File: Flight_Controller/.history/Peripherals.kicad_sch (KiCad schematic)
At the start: 56 parts, among them IC1 AT7456E, U2 BMI270, U3 TLV75533PDBV, U4 W25Q128JVSIQ TR, U6 LMR51625XDDCR, U8 LMR51625XDDCR, Y2 ABM3-27.000MHZ-D2Y-T

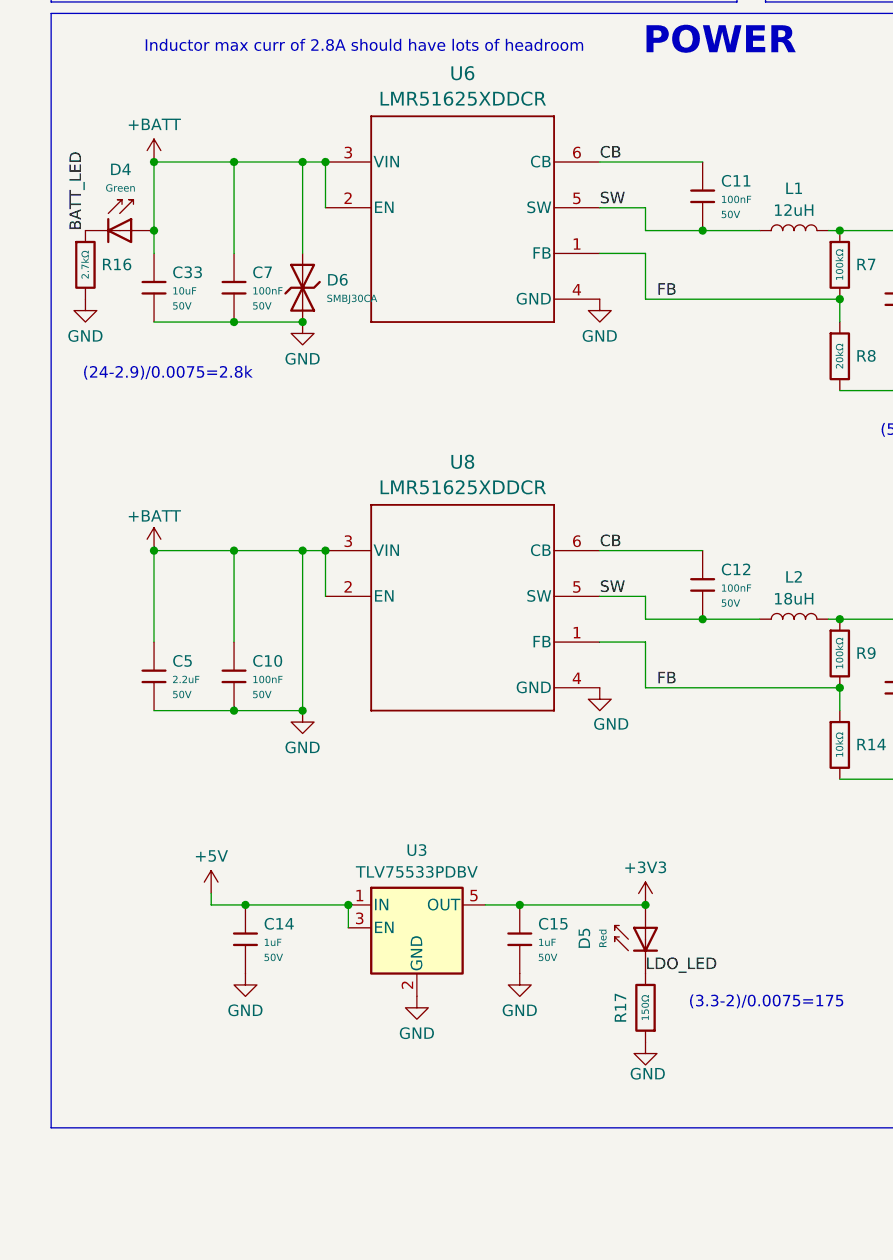
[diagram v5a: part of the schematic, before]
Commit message: Updated Footprints
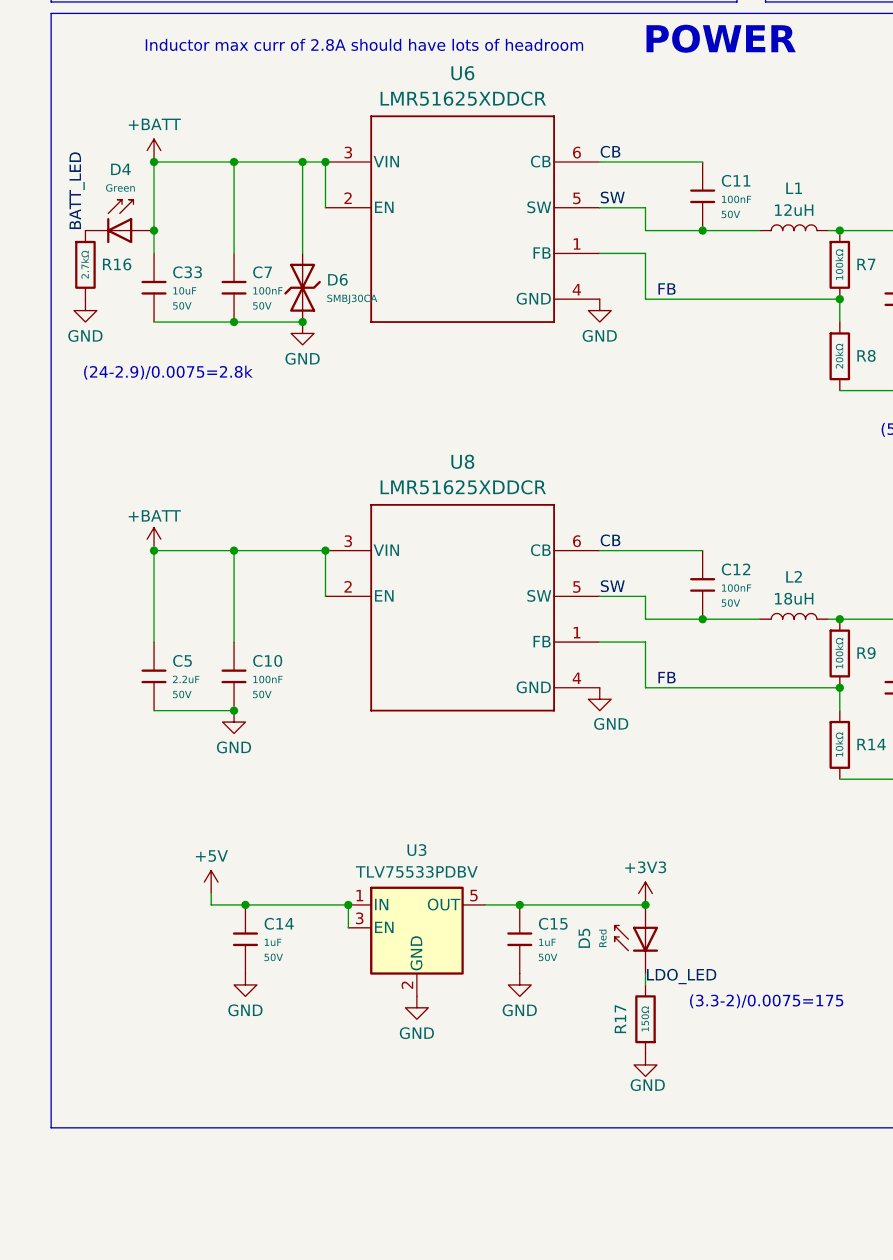
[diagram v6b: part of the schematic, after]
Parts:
- L2: footprint Inductor_SMD:L_TDK_VLS6045EX_VLS6045AF -> Inductor_SMD:L_TDK_VLP8040
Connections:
- net +BATT: no longer A1.3 (RES), A1.8 (GND_IO), A1.9 (GND), C10.2, C13.2, C14.2, C15.2, C24.2, C32.2, C33.2, C34.2, C35.2, C36.2, C37.2, C4.2, C5.2, C6.2, C7.2, C8.2, C9.2, D6.1, IC1.23 (PGND), IC1.29 (THERMALPAD), NT3.2, NT4.2, R14.2, R15.2, R16.2, R17.1, R18.2, R4.2, R8.2, U2.6 (GNDIO), U2.7 (GND), U3.2 (GND), U4.4 (GND), U6.4 (GND), U8.4 (GND)
- new net GND: A1.3 (RES), A1.8 (GND_IO), A1.9 (GND), C10.2, C13.2, C14.2, C15.2, C24.2, C32.2, C33.2, C34.2, C35.2, C36.2, C37.2, C4.2, C5.2, C6.2, C7.2, C8.2, C9.2, D6.1, IC1.23 (PGND), IC1.29 (THERMALPAD), NT3.2, NT4.2, R14.2, R15.2, R16.2, R17.1, R18.2, R4.2, R8.2, U2.6 (GNDIO), U2.7 (GND), U3.2 (GND), U4.4 (GND), U6.4 (GND), U8.4 (GND)
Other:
- moved on the sheet: R17

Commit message: Updated Layout to 60x30
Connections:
- net CB renamed CB_5V
- net CB_5V: no longer C12.1, U8.6 (CB)
- net FB renamed FB_5V
- net FB_5V: no longer R14.1, R9.2, U8.1 (FB)
- net SW renamed SW_5V
- net SW_5V: no longer C12.2, L2.1, U8.5 (SW)
- new net CB_9V: C12.1, U8.6 (CB)
- new net FB_9V: R14.1, R9.2, U8.1 (FB)
- new net SW_9V: C12.2, L2.1, U8.5 (SW)
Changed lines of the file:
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@@
 		)
 	)
-	(label "FB"
+	(label "FB_5V"
 		(at 81.28 104.14 0)
 		(effects
@@
 		)
 	)
-	(label "SW"
+	(label "SW_9V"
 		(at 74.93 137.16 0)
 		(effects
@@
 		)
 	)
-	(label "SW"
+	(label "SW_5V"
 		(at 74.93 93.98 0)
 		(effects
@@
 		)
 	)
-	(label "CB"
+	(label "CB_5V"
 		(at 74.93 88.9 0)
 		(effects
@@
 		)
 	)
-	(label "FB"
+	(label "FB_9V"
 		(at 81.28 147.32 0)
 		(effects
@@
 		)
 	)
-	(label "CB"
+	(label "CB_9V"
 		(at 74.93 132.08 0)
 		(effects

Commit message: Routing Done!
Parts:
- removed R1, R3: 1kΩ, PCM_JLCPCB:R_0603, symbol PCM_JLCPCB-Resistors:0603,1kΩ
- removed R14: 10kΩ, PCM_JLCPCB:R_0603, symbol PCM_JLCPCB-Resistors:0603,10kΩ
- removed R7: 100kΩ, PCM_JLCPCB:R_0603, symbol PCM_JLCPCB-Resistors:0603,100kΩ
- removed R8: 20kΩ, PCM_JLCPCB:R_0603, symbol PCM_JLCPCB-Resistors:0603,20kΩ
- added R1: 53.6K, PCM_JLCPCB:R_0603, symbol Device:R
- added R3: 10.2K, PCM_JLCPCB:R_0603, symbol Device:R
- added R7: 9.76K, PCM_JLCPCB:R_0603, symbol Device:R
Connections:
- net +5V: now also R1.1
- net FB_5V: now also R1.2, R3.1
- net FB_9V: now also R7.1
- net GND: now also R3.2, R7.2
- net SPI_SCK: no longer A1.2 (SCL/SPC), IC1.10 (SCLK)
- net SPI_SDI: no longer A1.4 (SDA/SDI/SDO), IC1.9 (SDIN)
- net SPI_SDO: no longer A1.5 (SDO/SA0), IC1.11 (SDOUT)
- net LPS_SPI_CS: no longer names the net of A1.6 (CS)
- net OSD_LOS: no longer names the net of IC1.12 (LOS)
- net OSD_VS: no longer names the net of IC1.17 (~{VSYNC})
- new net I2C_SCL1: A1.2 (SCL/SPC)
- new net I2C_SDA1: A1.4 (SDA/SDI/SDO)
- new net OSD_SPI_SCK: IC1.10 (SCLK)
- new net OSD_SPI_SDI: IC1.9 (SDIN)
- new net OSD_SPI_SDO: IC1.11 (SDOUT)
- no-connect marks 15 -> 19
